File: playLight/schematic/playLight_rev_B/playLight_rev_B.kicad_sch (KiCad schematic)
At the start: 30 parts, among them J1 Conn_01x01, J10 Conn_01x01, J2 Conn_01x01, J3 Conn_01x01, J4 Conn_01x01, J5 Conn_01x01, J6 Conn_01x01, J7 Conn_01x01, J8 Conn_01x01, J9 Conn_01x01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

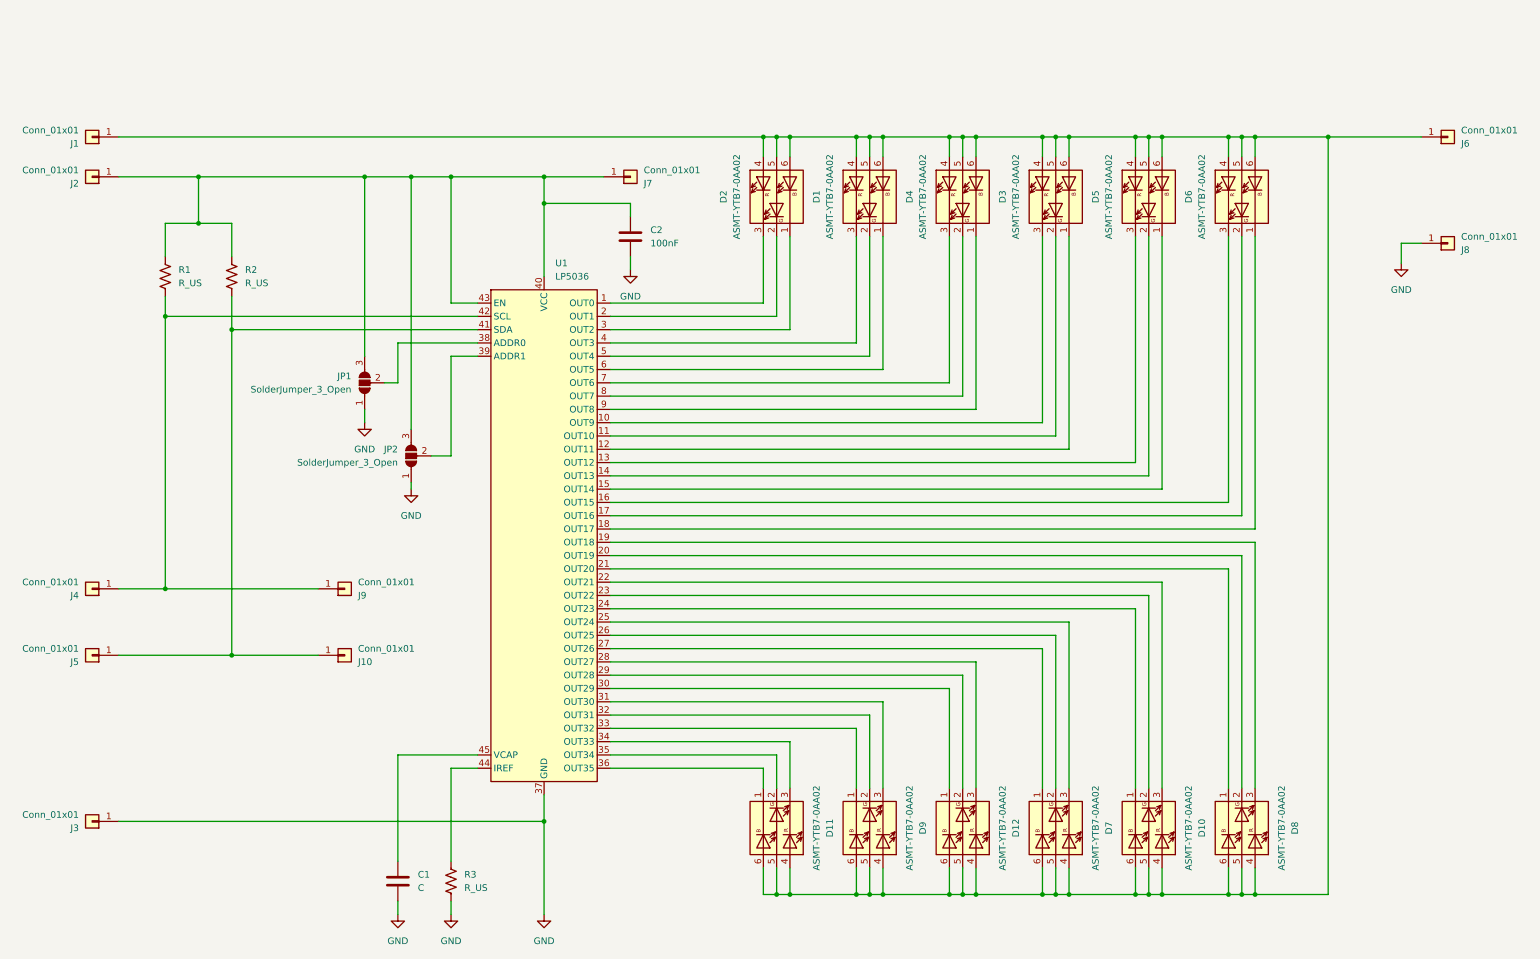
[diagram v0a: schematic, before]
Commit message: added a simplified revision replaced MCU with a 2x I2C support
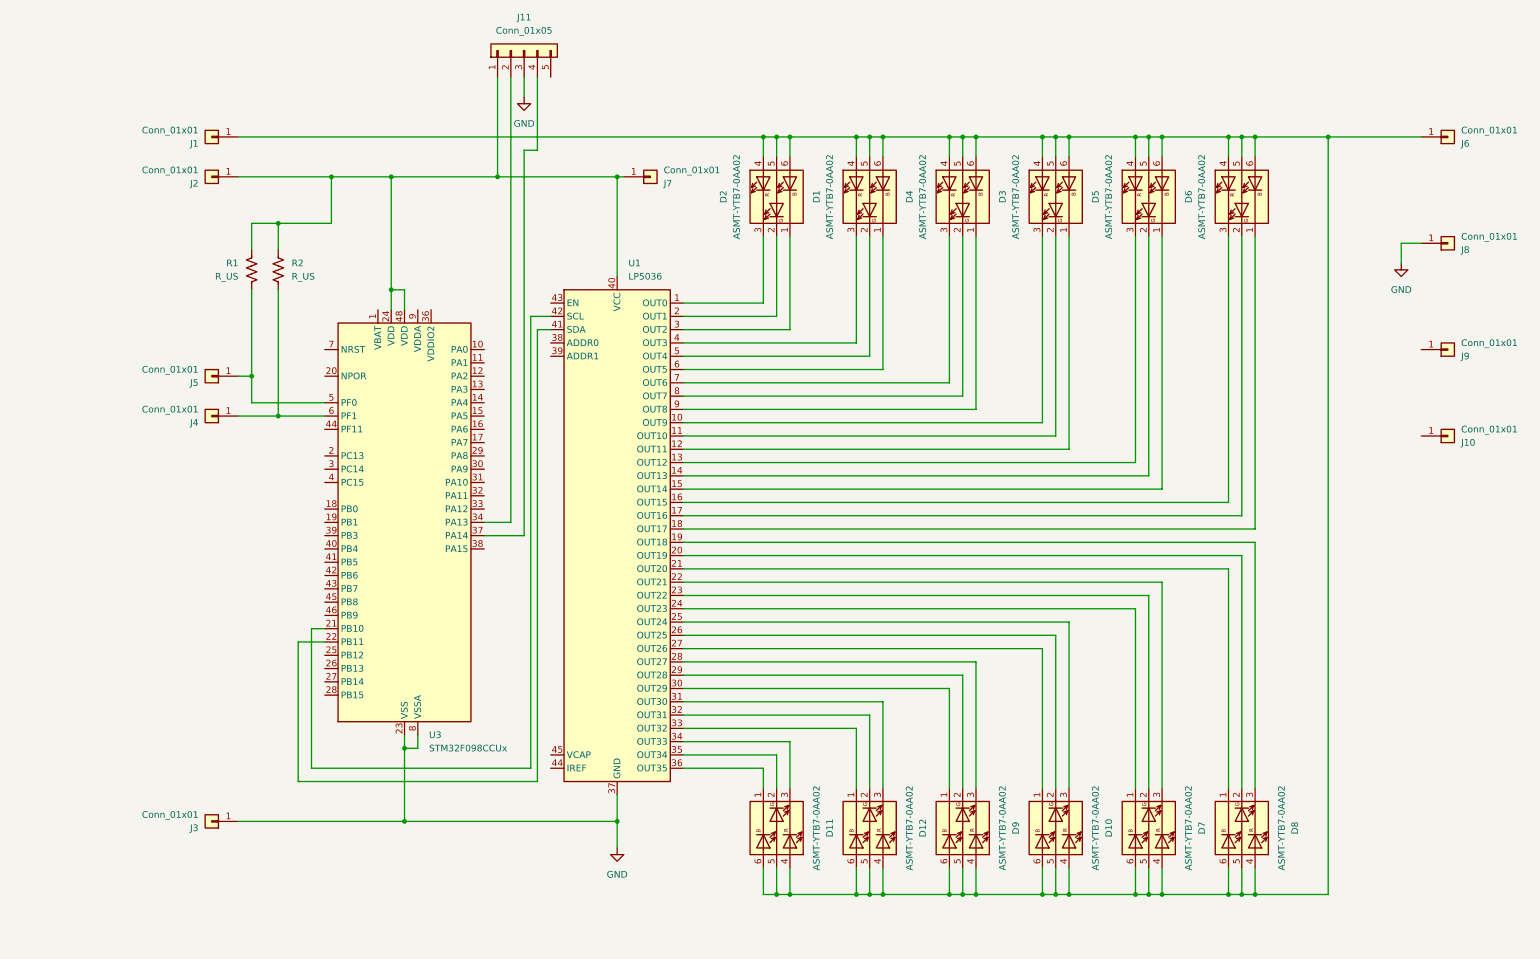
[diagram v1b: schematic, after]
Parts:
- removed C1: C, Capacitor_SMD:C_0805_2012Metric_Pad1.18x1.45mm_HandSolder, symbol Device:C
- removed C2: 100nF, Capacitor_SMD:C_0805_2012Metric_Pad1.18x1.45mm_HandSolder, symbol Device:C
- removed JP1, JP2: SolderJumper_3_Open, Jumper:SolderJumper-3_P1.3mm_Open_RoundedPad1.0x1.5mm, symbol Jumper:SolderJumper_3_Open
- removed R3: R_US, Resistor_SMD:R_0603_1608Metric_Pad0.98x0.95mm_HandSolder, symbol Device:R_US
- added J11: Conn_01x05, Connector_PinHeader_2.00mm:PinHeader_1x05_P2.00mm_Horizontal, symbol Connector_Generic:Conn_01x05
- added U3: STM32F098CCUx, Package_DFN_QFN:QFN-48-1EP_7x7mm_P0.5mm_EP5.6x5.6mm, symbol MCU_ST_STM32F0:STM32F098CCUx
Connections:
- net GND: now also J11.3 (Pin_3), U3.23 (VSS), U3.35 (VSS), U3.47 (VSS), U3.49 (VSS), U3.8 (VSSA)
- net at D7.1 (KB): now also U1.24 (OUT23); no longer U1.27 (OUT26)
- net at D7.2 (KG): now also U1.23 (OUT22); no longer U1.26 (OUT25)
- net at D7.3 (KR): now also U1.22 (OUT21); no longer U1.25 (OUT24)
- net at J2.1 (Pin_1), J7.1 (Pin_1), R1.1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: now also J11.1 (Pin_1), U3.24 (VDD), U3.48 (VDD); no longer U1.43 (EN)
- net at D10.1 (KB): now also U1.27 (OUT26); no longer U1.24 (OUT23)
- net at D10.2 (KG): now also U1.26 (OUT25); no longer U1.23 (OUT22)
- net at D10.3 (KR): now also U1.25 (OUT24); no longer U1.22 (OUT21)
- net at U1.28 (OUT27): now also D9.3 (KR); no longer D12.3 (KR)
- net at U1.29 (OUT28): now also D9.2 (KG); no longer D12.2 (KG)
- net at U1.30 (OUT29): now also D9.1 (KB); no longer D12.1 (KB)
- net at U1.31 (OUT30): now also D12.3 (KR); no longer D9.3 (KR)
- net at U1.32 (OUT31): now also D12.2 (KG); no longer D9.2 (KG)
- net at U1.33 (OUT32): now also D12.1 (KB); no longer D9.1 (KB)
- new net: J4.1 (Pin_1), R2.2, U3.6 (PF1)
- new net: J5.1 (Pin_1), R1.2, U3.5 (PF0)
- new net: U1.41 (SDA), U3.22 (PB11)
- new net: U1.42 (SCL), U3.21 (PB10)
- new net: J11.2 (Pin_2), U3.34 (PA13)
- new net: J11.4 (Pin_4), U3.37 (PA14)
- now unconnected: J10.1 (Pin_1), J9.1 (Pin_1)
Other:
- moved on the sheet: D10, D12, D7, D9, J1, J10, J2, J3, J4, J5, J7, J9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
